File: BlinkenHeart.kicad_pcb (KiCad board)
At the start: 2 copper layers, 23 parts, among them IC1 ATTINY85-S, SW1 SW_Push, SW2 On-Switch

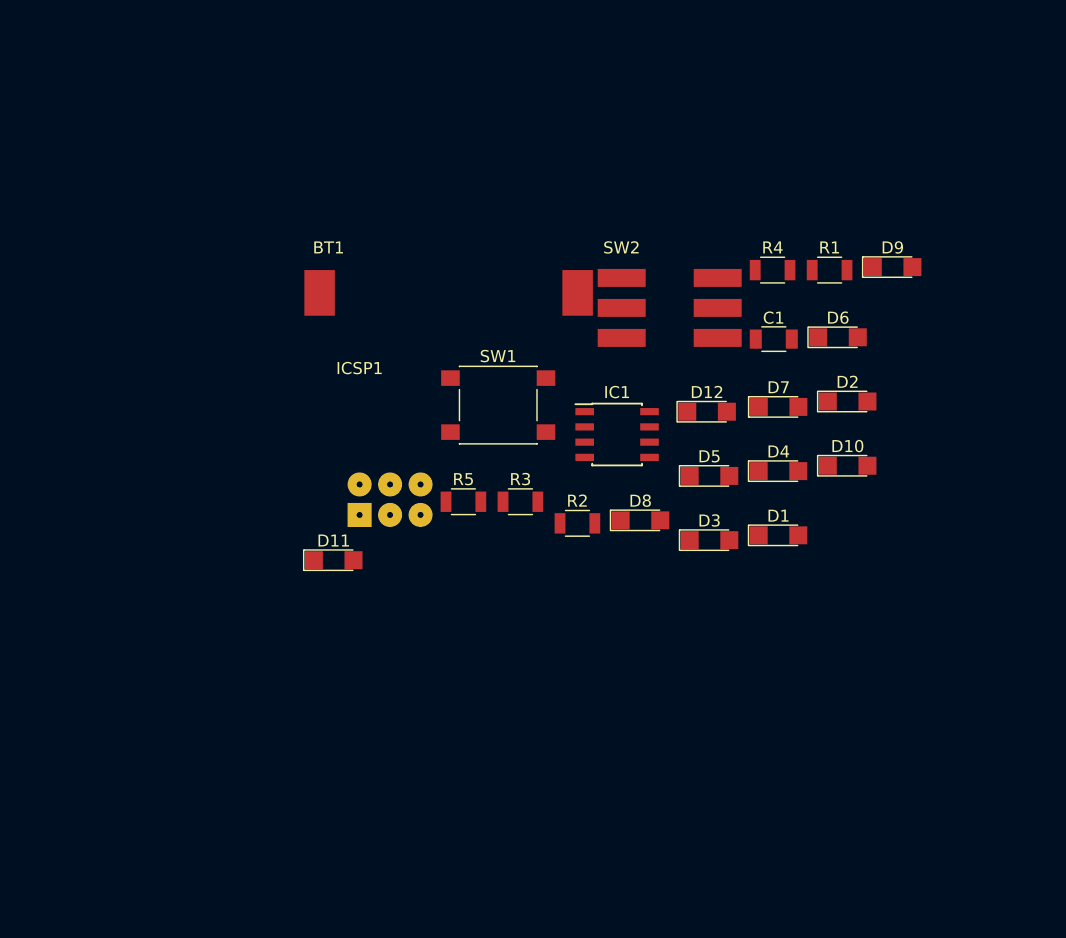
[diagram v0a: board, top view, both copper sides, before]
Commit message: finished border-cuts and routing
border-cuts is now a mathematicaly correct defined heart (thanks Mathias)
routing is complete, but needs some aesthetic changes
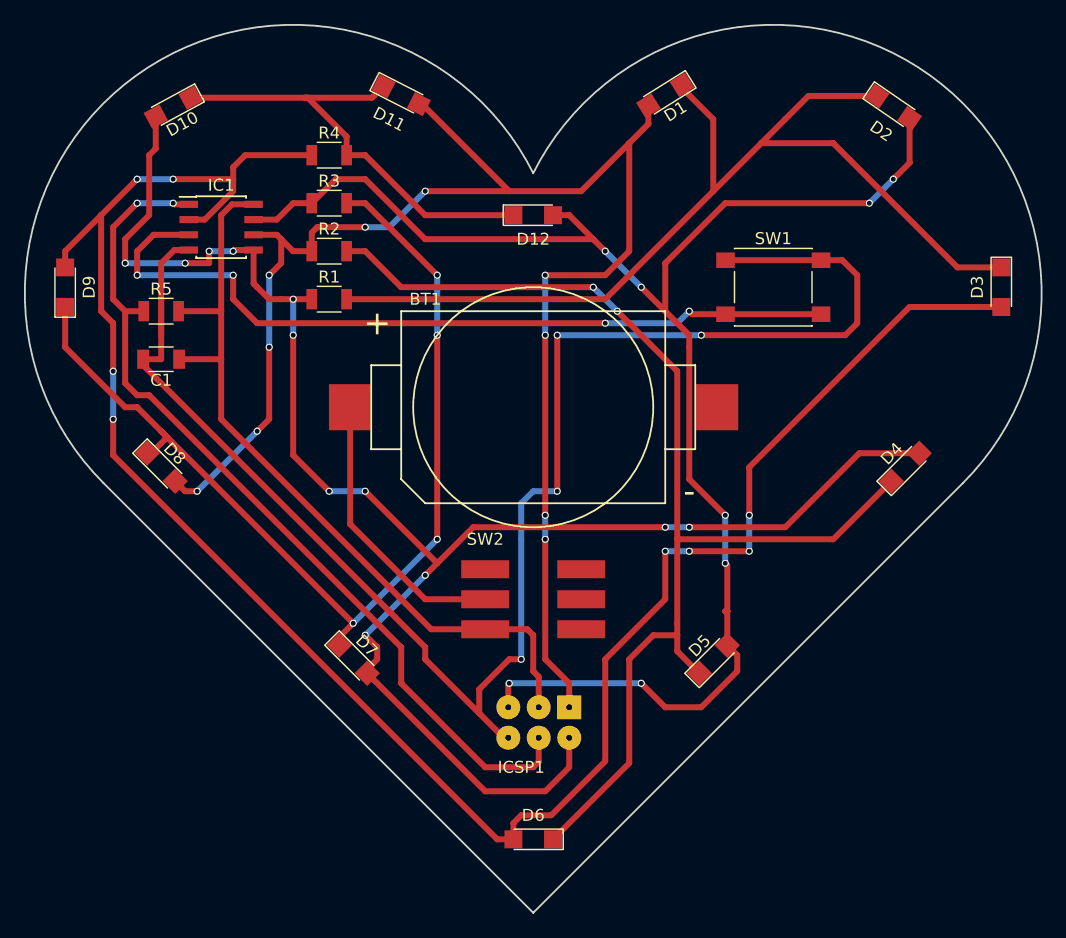
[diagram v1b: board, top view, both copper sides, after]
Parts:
- moved D9 69.0 mm to (143.0, 106.0), turned to 90 degrees
- moved D10 63.6 mm to (152.0, 91.0), turned to 208.5 degrees
- moved C1 51.1 mm to (151.0, 112.0), turned to 180 degrees
- moved D6 48.9 mm to (182.0, 152.0), turned to 180 degrees
- moved R1 41.8 mm to (165.0, 107.0)
- moved D7 41.2 mm to (167.0, 137.0), turned to 315 degrees
- moved D8 40.2 mm to (151.0, 121.0), turned to 315 degrees
- moved D11 39.2 mm to (171.0, 90.0), turned to 333 degrees
- moved R4 38.2 mm to (165.0, 95.0)
- moved D1 37.9 mm to (193.0, 90.0), turned to 212 degrees
- moved IC1 37.2 mm to (156.0, 101.0)
- moved D3 32.2 mm to (221.0, 106.0), turned to 270 degrees
- moved R2 30.7 mm to (165.0, 103.0)
- moved R5 29.8 mm to (151.0, 108.0)
- moved R3 29.5 mm to (165.0, 99.0)
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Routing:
- net 4: track 0.00 -> 169.7 mm, vias 0 -> 8
- net 1: track 0.00 -> 142.5 mm, vias 0 -> 12
- net GND: track 0.00 -> 136.5 mm, vias 0 -> 4
- net 3: track 0.00 -> 132.0 mm, vias 0 -> 8
- net 2: track 0.00 -> 130.6 mm, vias 0 -> 10
- net Net-(D4-Pad1): track 0.00 -> 99.9 mm, vias 0 -> 2
- net Net-(D1-Pad1): track 0.00 -> 85.4 mm
- net Net-(D7-Pad1): track 0.00 -> 84.3 mm, vias 0 -> 4
- net RST: track 0.00 -> 73.8 mm, vias 0 -> 2
- net Net-(IC1-Pad3): track 0.00 -> 67.5 mm, vias 0 -> 4
- net VCC: track 0.00 -> 66.8 mm
- net Net-(D10-Pad1): track 0.00 -> 38.8 mm
- net Net-(BT1-Pad1): track 0.00 -> 23.6 mm
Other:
- board outline added: 84.7 x 74 mm
- net class Default: trace_width 0.25 -> 0.5
- net class VCC added: clearance 0.2, trace_width 0.5, via_dia 0.6, via_drill 0.4

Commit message: fixed ground-connection to battery-holder and made some aesthethik changes to the routing
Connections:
- BT1 pad 2: (no net) -> GND
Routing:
- net GND: track 136.5 -> 142.4 mm
- net Net-(D4-Pad1): track 99.9 -> 99.3 mm
- net 2: track 130.6 -> 130.0 mm

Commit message: added fablab-neuenstadt logo
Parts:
- added G***: LOGO, logo:logo, F.Cu at (182.0, 116.0)

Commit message: moved net 3 away from ground-pin of the battery-holder
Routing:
- net Net-(D4-Pad1): track 99.3 -> 100.9 mm
- net 4: track 169.7 -> 170.3 mm

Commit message: Fixed the ICSP Header
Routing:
- net VCC: track 66.8 -> 75.5 mm, vias 0 -> 2
- net RST: track 73.8 -> 65.2 mm, vias 2 -> 4
- net 1: track 142.5 -> 138.5 mm
- net 3: track 132.5 -> 128.9 mm
- net GND: track 142.4 -> 143.3 mm

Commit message: Fixed the Attiny footprint
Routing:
- net 1: track 138.5 -> 141.8 mm
- net VCC: track 75.5 -> 76.3 mm
- net Net-(IC1-Pad3): track 67.5 -> 66.8 mm
- net 4: track 170.3 -> 171.1 mm
- net GND: track 143.3 -> 142.6 mm
- net 3: track 128.9 -> 128.2 mm
- net RST: track 65.2 -> 65.8 mm
- net 2: track 130.0 -> 129.6 mm, vias 10 -> 8

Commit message: Added some holes, fixed some other minor things. Also: Added a logo and did some rerouting
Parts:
- removed the G*** at (182.0, 116.0)
- added ?: , single_pad:single_pad, F.Cu at (201.9, 88.1)
- added ?: , single_pad:single_pad, F.Cu at (161.3, 88.1)
- added D13: D_Schottky, Diodes_SMD:D_1206, F.Cu at (169.2, 126.2)
- added G***: LOGO, logo:logo, F.Cu at (212.3, 107.2)
- added G***: LOGO, logo:logo, B.Cu at (201.2, 116.8)
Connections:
- SW2 pad 2: Net-(BT1-Pad1) -> Net-(D13-Pad1)
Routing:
- net Net-(BT1-Pad1): track 23.6 -> 9.76 mm
- net Net-(D13-Pad1): track 0.00 -> 9.67 mm
- net Net-(D10-Pad1): track 38.8 -> 36.9 mm
- net 1: track 141.8 -> 142.6 mm
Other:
- board text added: "FABLAB NEUENSTADT BLINKENHEART.DE"

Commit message: Next prototype version blah blah blah
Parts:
- removed the G*** at (212.3, 107.2)
- removed the G*** at (201.2, 116.8)
- added G***: LOGO, logo:logo, F.Cu at (272.5, 34.0)
- added G***: LOGO, arrow:arrow, F.Cu at (259.6, 58.2)
- BT1: value 3.3V CR3032 -> 3.3V CR2032; footprint CR3032-Holder:CR3032-Holder -> CR2032-Holder:CR2032-Holder
- C1: value 1 μF -> 1μF
- D13: value D_Schottky -> D13
- ICSP1: value CONN_01X06 -> ISP
- SW1: value SW_Push -> Taster
- SW2: value On-Switch -> Schalter
- moved ? 109.5 mm to (232.9, 5.33)
- moved ? 109.5 mm to (273.6, 5.33)
- moved BT1 109.5 mm to (236.6, 33.2)
- moved C1 109.5 mm to (222.6, 29.2)
- moved D1 109.5 mm to (264.6, 7.20)
- moved D10 109.5 mm to (223.6, 8.20)
- moved D11 109.5 mm to (242.6, 7.20)
- moved D12 109.5 mm to (253.6, 17.2)
- moved D13 109.5 mm to (240.8, 43.4)
- moved D2 109.5 mm to (283.6, 8.20)
- moved D3 109.5 mm to (292.6, 23.2)
- moved D4 109.5 mm to (284.6, 38.2)
- moved D5 109.5 mm to (268.6, 54.2)
- moved D6 109.5 mm to (253.6, 69.2)
- moved D7 109.5 mm to (238.6, 54.2)
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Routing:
- net RST: vias 4 -> 3
- net 3: vias 8 -> 7
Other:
- board text added: "an"
